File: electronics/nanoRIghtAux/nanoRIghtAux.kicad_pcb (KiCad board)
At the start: 2 copper layers, 16 parts, among them J1 Conn_02x03_Counter_Clockwise, J10 Conn_02x03_Counter_Clockwise, J11 Conn_01x03_Socket, J2 Conn_01x03_Pin, J3 Conn_01x03_Pin, J4 Conn_01x03_Pin, J5 Conn_01x03_Pin, J6 Conn_01x04_Socket, J7 Conn_01x04_Socket, J8 Conn_01x04_Socket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

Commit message: PCB edit started
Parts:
- J1: value Conn_02x03_Counter_Clockwise -> Conn_MM5451
- J10: value Conn_02x03_Counter_Clockwise -> Conn_EA_GLCD
- J11: value Conn_01x03_Socket -> Conn_MAX7219
- J2: value Conn_01x03_Pin -> Conn_HYDA
- J3: value Conn_01x03_Pin -> Conn_HYDB
- J4: value Conn_01x03_Pin -> Conn_FUEL_FR
- J5: value Conn_01x03_Pin -> Conn_FUEL_AL
- J6: value Conn_01x04_Socket -> Conn_MOT_D
- J7: value Conn_01x04_Socket -> Conn_MOT_C
- J8: value Conn_01x04_Socket -> Conn_MOT_B
- J9: value Conn_01x04_Socket -> Conn_MOT_A
- moved SW3 62.9 mm to (199.4, 61.5)
- moved J6 52.6 mm to (223.5, 100.3), turned to 180 degrees
- moved SW2 48.9 mm to (188.9, 65.3), turned to -90 degrees
- moved J10 43.1 mm to (154.9, 85.1), turned to -90 degrees
- moved J7 41.1 mm to (205.7, 121.9), turned to -90 degrees
- moved SW1 41.1 mm to (177.8, 64.8), turned to 180 degrees
- moved J11 40.6 mm to (155.0, 113.0)
- moved J5 39.7 mm to (154.9, 109.2), turned to -90 degrees
- moved J9 39.6 mm to (223.5, 104.1)
- moved J1 35.1 mm to (154.9, 91.4), turned to -90 degrees
- moved J4 33.6 mm to (154.9, 105.4), turned to -90 degrees
- moved J3 27.6 mm to (154.9, 101.6), turned to -90 degrees
- moved U3 26.9 mm to (201.1, 104.8), turned to 180 degrees
- moved J2 21.6 mm to (154.9, 97.8), turned to -90 degrees
- moved J8 18.8 mm to (196.9, 83.8), turned to 90 degrees
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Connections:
- J1 pad 1: unconnected-(J1-Pin_1-Pad1) -> Net-(A1-D4)
- J1 pad 2: unconnected-(J1-Pin_2-Pad2) -> Net-(A1-D5)
- J1 pad 3: Net-(A1-D5) -> +5V
- J1 pad 4: Net-(A1-D4) -> unconnected-(J1-Pin_4-Pad4)
- J1 pad 5: +5V -> GND
- J1 pad 6: GND -> unconnected-(J1-Pin_6-Pad6)
- J10 pad 1: unconnected-(J10-Pin_1-Pad1) -> Net-(A1-D2)
- J10 pad 2: unconnected-(J10-Pin_2-Pad2) -> Net-(A1-D3)
- J10 pad 3: Net-(A1-D3) -> +5V
- J10 pad 4: Net-(A1-D2) -> unconnected-(J10-Pin_4-Pad4)
- J10 pad 5: +5V -> GND
- J10 pad 6: GND -> unconnected-(J10-Pin_6-Pad6)

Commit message: PWR input pinheader added, MAX7219_PWR pinheader added, PCB routing changed
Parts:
- added J12: Conn_PWRInput, Connector_PinHeader_2.54mm:PinHeader_1x02_P2.54mm_Vertical, F.Cu at (147.3, 121.9)
- added J13: Conn_MAX_Pwr, Connector_PinSocket_2.54mm:PinSocket_1x02_P2.54mm_Vertical, F.Cu at (147.3, 115.6)
- SW1, SW2, SW3: footprint Button_Switch_THT:SW_PUSH_6mm -> Connector_PinHeader_2.54mm:PinHeader_1x02_P2.54mm_Vertical
- moved SW3 28.5 mm to (171.4, 67.3)
- moved J7 23.3 mm to (196.8, 100.3), turned to 180 degrees
- moved J8 20.3 mm to (196.8, 104.2), turned to 0 degrees
- moved SW2 12.6 mm to (176.5, 67.3), turned to 0 degrees
- moved SW1 12.5 mm to (166.4, 69.8)
- moved U3 10.2 mm to (210.8, 101.6)
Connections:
- U3 pad 10: Net-(J6-Pin_4) -> Net-(J6-Pin_3)
- U3 pad 11: Net-(J6-Pin_3) -> Net-(J6-Pin_4)
- U3 pad 18: Net-(J7-Pin_3) -> Net-(J7-Pin_4)
- U3 pad 19: Net-(J7-Pin_4) -> Net-(J7-Pin_3)
- U3 pad 24: Net-(J8-Pin_4) -> Net-(J8-Pin_3)
- U3 pad 25: Net-(J8-Pin_3) -> Net-(J8-Pin_4)
- U3 pad 4: Net-(J9-Pin_3) -> Net-(J9-Pin_4)
- U3 pad 5: Net-(J9-Pin_4) -> Net-(J9-Pin_3)
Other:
- board outline added: 101.6 x 94 mm

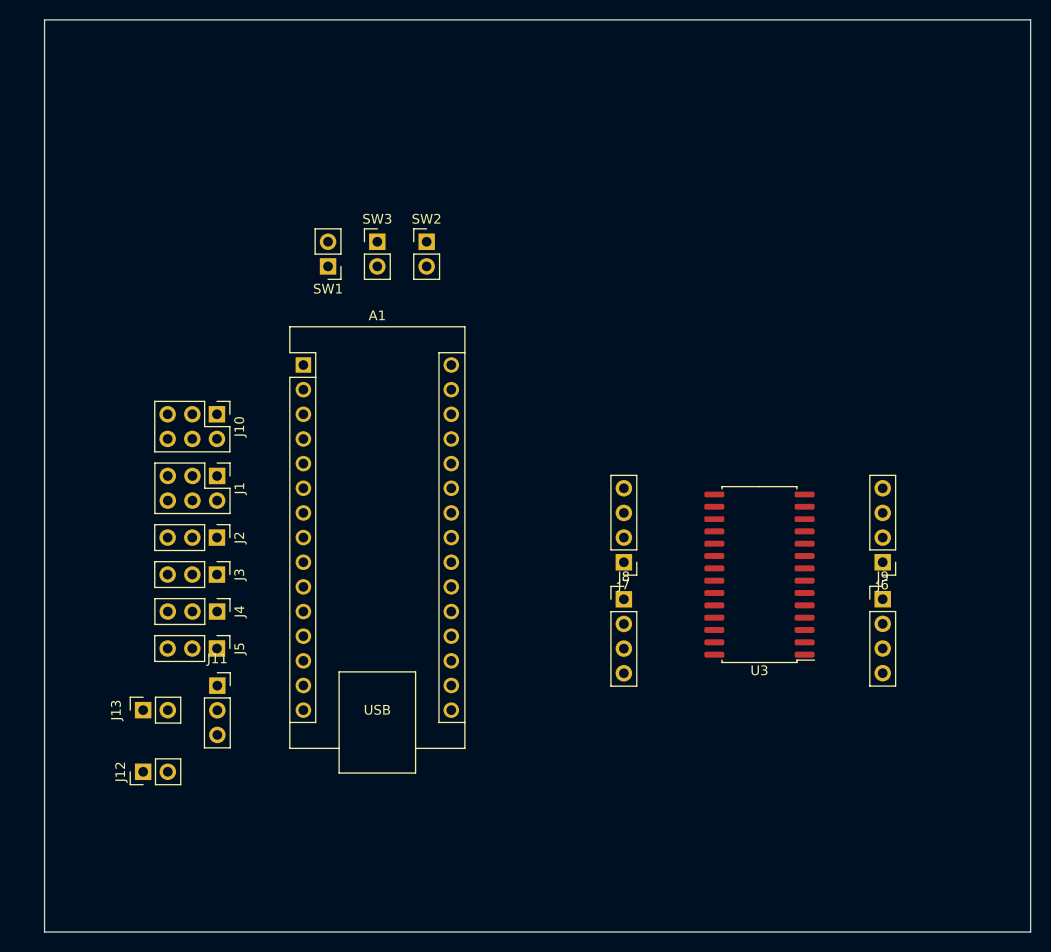
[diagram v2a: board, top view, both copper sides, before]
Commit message: first routing of TH components done.
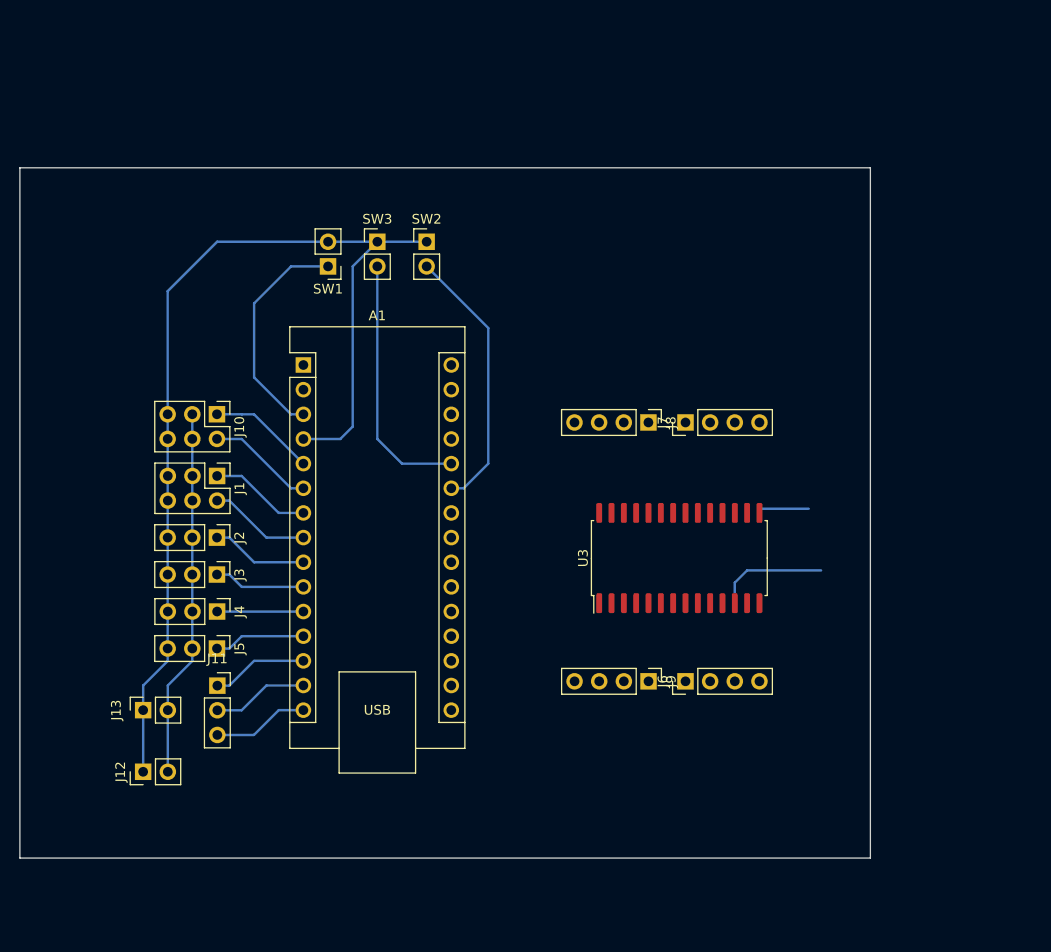
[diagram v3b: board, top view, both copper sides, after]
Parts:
- moved J9 25.6 mm to (199.4, 112.6), turned to -90 degrees
- moved J6 23.7 mm to (203.2, 112.6), turned to 90 degrees
- moved J8 18.4 mm to (199.4, 85.9), turned to -90 degrees
- moved J7 15.7 mm to (203.2, 85.9), turned to 90 degrees
- moved U3 8.43 mm to (202.6, 99.9), turned to 90 degrees
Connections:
- J1 pad 4: unconnected-(J1-Pin_4-Pad4) -> +5V
- J1 pad 6: unconnected-(J1-Pin_6-Pad6) -> GND
- J10 pad 4: unconnected-(J10-Pin_4-Pad4) -> +5V
- J10 pad 6: unconnected-(J10-Pin_6-Pad6) -> GND
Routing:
- net GND: track 0.00 -> 110.1 mm
- net +5V: track 0.00 -> 48.6 mm
- net Net-(A1-A6): track 0.00 -> 27.8 mm
- net Net-(A1-A7): track 0.00 -> 26.5 mm
- net Net-(A1-~{RESET}-Pad3): track 0.00 -> 23.5 mm
- net Net-(A1-D3): track 0.00 -> 11.0 mm
- net Net-(A1-D2): track 0.00 -> 11.0 mm
- net Net-(A1-D5): track 0.00 -> 10.5 mm
- net Net-(A1-D4): track 0.00 -> 10.5 mm
- net Net-(A1-D6): track 0.00 -> 9.96 mm
- net Net-(A1-D12): track 0.00 -> 9.92 mm
- net Net-(A1-D10): track 0.00 -> 9.92 mm
- net Net-(A1-D11): track 0.00 -> 9.92 mm
- net Net-(A1-D7): track 0.00 -> 9.43 mm
- net Net-(A1-D9): track 0.00 -> 9.43 mm
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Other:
- board size 101.6 x 94 mm -> 87.6 x 71.1 mm

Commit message: routing cleanup of TH components
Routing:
- net +5V: track 48.6 -> 37.9 mm
- net GND: track 110.1 -> 105.1 mm
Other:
- board text added: "RightAUX Control Board"
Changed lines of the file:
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@@
     (pad_to_mask_clearance 0)
     (pcbplotparams
-      (layerselection 0x00010fc_ffffffff)
+      (layerselection 0x0000000_fffffffe)
       (plot_on_all_layers_selection 0x0000000_00000000)
       (disableapertmacros false)
@@
       (outputformat 1)
       (mirror false)
-      (drillshape 1)
+      (drillshape 0)
       (scaleselection 1)
-      (outputdirectory "")
+      (outputdirectory "/media/michi/miWorkdata/myproject/F-16SimulatorParts/BMSAIT-RightAux/electronics/nanoRIghtAux/")
     )
   )
@@
   (gr_rect (start 134.62 59.69) (end 222.25 130.81)
     (stroke (width 0.1) (type default)) (fill none) (layer "Edge.Cuts"))
+  (gr_text "RightAUX Control Board" (at 161.29 127) (layer "B.SilkS")
+    (effects (font (size 2 2) (thickness 0.15)) (justify left bottom))
+  )
   (segment (start 166.37 69.85) (end 162.56 69.85) (width 0.25) (layer "B.Cu") (net 3))
   (segment (start 158.75 81.28) (end 158.75 73.66) (width 0.25) (layer "B.Cu") (net 3))
@@
   (segment (start 171.45 67.31) (end 168.91 69.85) (width 0.25) (layer "B.Cu") (net 4))
   (segment (start 166.37 67.31) (end 154.94 67.31) (width 0.25) (layer "B.Cu") (net 4))
-  (segment (start 215.9 94.82) (end 210.82 94.82) (width 0.25) (layer "B.Cu") (net 4))
   (segment (start 149.845 110.505) (end 147.32 113.03) (width 0.25) (layer "B.Cu") (net 4))
   (segment (start 168.91 69.85) (end 168.91 86.36) (width 0.25) (layer "B.Cu") (net 4))
@@
   (segment (start 171.45 87.63) (end 173.99 90.17) (width 0.25) (layer "B.Cu") (net 26))
   (segment (start 173.99 90.17) (end 179.07 90.17) (width 0.25) (layer "B.Cu") (net 26))
-  (segment (start 217.17 101.17) (end 209.55 101.17) (width 0.25) (layer "B.Cu") (net 30))
   (segment (start 152.385 85.085) (end 152.385 109.22) (width 0.25) (layer "B.Cu") (net 30))
   (segment (start 152.385 110.505) (end 149.86 113.03) (width 0.25) (layer "B.Cu") (net 30))
-  (segment (start 208.28 102.44) (end 208.28 103.71) (width 0.25) (layer "B.Cu") (net 30))
-  (segment (start 209.55 101.17) (end 208.28 102.44) (width 0.25) (layer "B.Cu") (net 30))
   (segment (start 149.86 113.03) (end 149.86 121.92) (width 0.25) (layer "B.Cu") (net 30))
   (segment (start 152.385 109.22) (end 152.385 110.505) (width 0.25) (layer "B.Cu") (net 30))

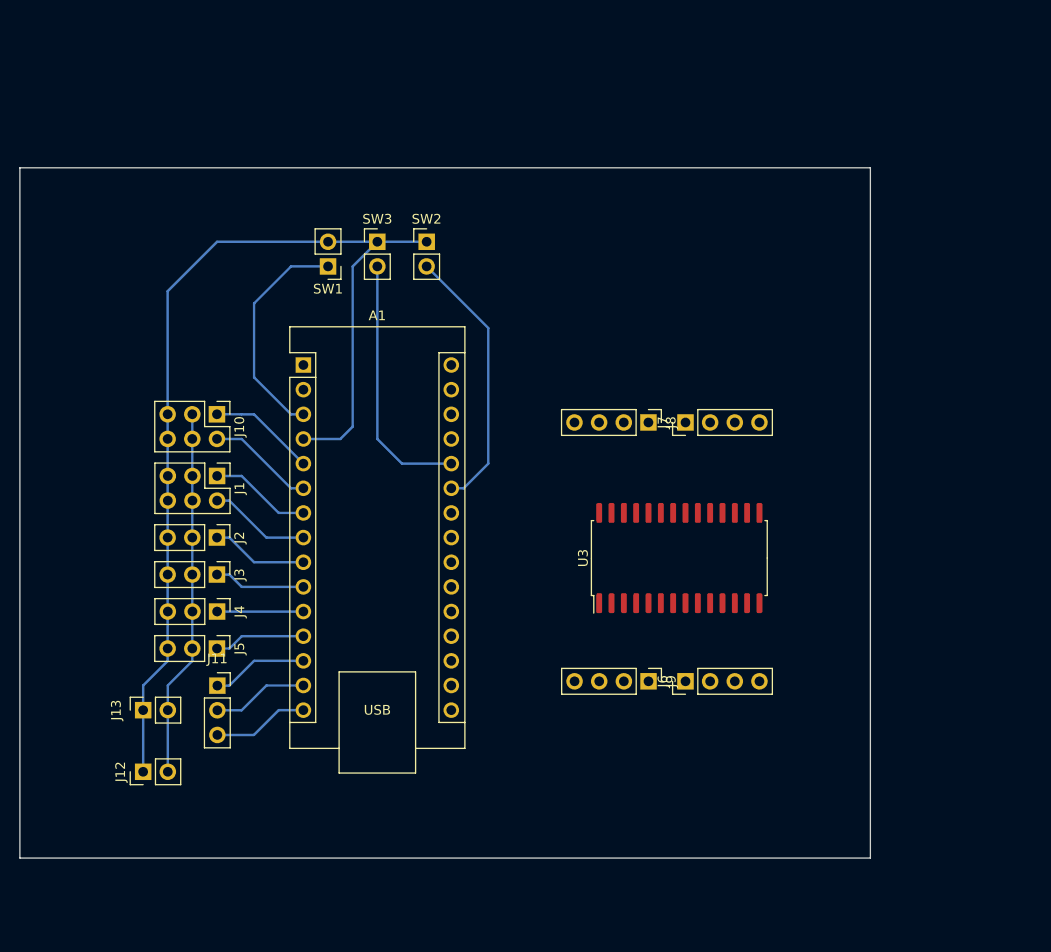
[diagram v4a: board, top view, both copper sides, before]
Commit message: mountingholes addes
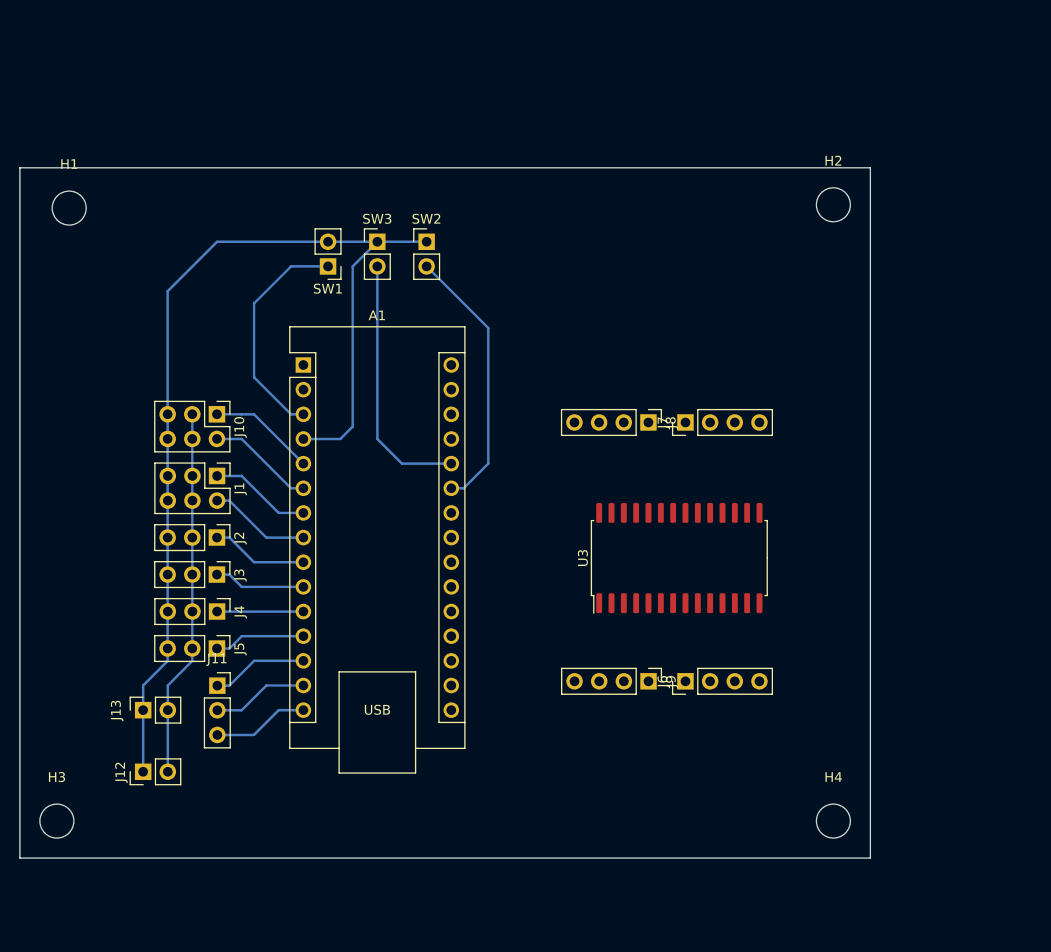
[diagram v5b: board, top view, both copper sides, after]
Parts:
- added H1: MountingHole, MountingHole:MountingHole_3.5mm, F.Cu at (139.7, 63.8)
- added H2: MountingHole, MountingHole:MountingHole_3.5mm, F.Cu at (218.4, 63.5)
- added H3: MountingHole, MountingHole:MountingHole_3.5mm, F.Cu at (138.4, 127.0)
- added H4: MountingHole, MountingHole:MountingHole_3.5mm, F.Cu at (218.4, 127.0)
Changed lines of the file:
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@@
     )
+  )
+  (footprint "MountingHole:MountingHole_3.5mm" (layer "F.Cu")
+    (at 139.7 63.84)
+    (descr "Mounting Hole 3.5mm, no annular")
+    (tags "mounting hole 3.5mm no annular")
+    (property "Sheetfile" "nanoRIghtAux.kicad_sch")
+    (property "Sheetname" "")
+    (property "ki_description" "Mounting Hole without connection")
+    (property "ki_keywords" "mounting hole")
+    (attr exclude_from_pos_files)
+    (fp_text reference "H1" (at 0 -4.5) (layer "F.SilkS")
+        (effects (font (size 1 1) (thickness 0.15)))
+    )
+    (fp_text value "MountingHole" (at 0 4.5) (layer "F.Fab")
+        (effects (font (size 1 1) (thickness 0.15)))
+    )
+    (fp_text user "${REFERENCE}" (at 0 0) (layer "F.Fab")
+        (effects (font (size 1 1) (thickness 0.15)))
+    )
+    (fp_circle (center 0 0) (end 3.5 0)
+      (stroke (width 0.15) (type solid)) (fill none) (layer "Cmts.User"))
+    (fp_circle (center 0 0) (end 3.75 0)
+      (stroke (width 0.05) (type solid)) (fill none) (layer "F.CrtYd"))
+    (pad "" np_thru_hole circle (at 0 0) (size 3.5 3.5) (drill 3.5) (layers "*.Cu" "*.Mask"))
   )
   (footprint "Connector_PinHeader_2.54mm:PinHeader_1x04_P2.54mm_Vertical" (layer "F.Cu")
@@
       (rotate (xyz 0 0 0))
     )
+  )
+  (footprint "MountingHole:MountingHole_3.5mm" (layer "F.Cu")
+    (at 218.44 127)
+    (descr "Mounting Hole 3.5mm, no annular")
+    (tags "mounting hole 3.5mm no annular")
+    (property "Sheetfile" "nanoRIghtAux.kicad_sch")
+    (property "Sheetname" "")
+    (property "ki_description" "Mounting Hole without connection")
+    (property "ki_keywords" "mounting hole")
+    (attr exclude_from_pos_files)
+    (fp_text reference "H4" (at 0 -4.5) (layer "F.SilkS")
+        (effects (font (size 1 1) (thickness 0.15)))
+    )
+    (fp_text value "MountingHole" (at 0 4.5) (layer "F.Fab")
+        (effects (font (size 1 1) (thickness 0.15)))
+    )
+    (fp_text user "${REFERENCE}" (at 0 0) (layer "F.Fab")
+        (effects (font (size 1 1) (thickness 0.15)))
+    )
+    (fp_circle (center 0 0) (end 3.5 0)
+      (stroke (width 0.15) (type solid)) (fill none) (layer "Cmts.User"))
+    (fp_circle (center 0 0) (end 3.75 0)
+      (stroke (width 0.05) (type solid)) (fill none) (layer "F.CrtYd"))
+    (pad "" np_thru_hole circle (at 0 0) (size 3.5 3.5) (drill 3.5) (layers "*.Cu" "*.Mask"))
   )
   (footprint "Connector_PinHeader_2.54mm:PinHeader_1x04_P2.54mm_Vertical" (layer "F.Cu")
@@
     )
   )
+  (footprint "MountingHole:MountingHole_3.5mm" (layer "F.Cu")
+    (at 218.44 63.5)
+    (descr "Mounting Hole 3.5mm, no annular")
+    (tags "mounting hole 3.5mm no annular")
+    (property "Sheetfile" "nanoRIghtAux.kicad_sch")
+    (property "Sheetname" "")
+    (property "ki_description" "Mounting Hole without connection")
+    (property "ki_keywords" "mounting hole")
+    (attr exclude_from_pos_files)
+    (fp_text reference "H2" (at 0 -4.5) (layer "F.SilkS")
+        (effects (font (size 1 1) (thickness 0.15)))
+    )
+    (fp_text value "MountingHole" (at 0 4.5) (layer "F.Fab")
+        (effects (font (size 1 1) (thickness 0.15)))
+    )
+    (fp_text user "${REFERENCE}" (at 0 0) (layer "F.Fab")
+        (effects (font (size 1 1) (thickness 0.15)))
+    )
+    (fp_circle (center 0 0) (end 3.5 0)
+      (stroke (width 0.15) (type solid)) (fill none) (layer "Cmts.User"))
+    (fp_circle (center 0 0) (end 3.75 0)
+      (stroke (width 0.05) (type solid)) (fill none) (layer "F.CrtYd"))
+    (pad "" np_thru_hole circle (at 0 0) (size 3.5 3.5) (drill 3.5) (layers "*.Cu" "*.Mask"))
+  )
+  (footprint "MountingHole:MountingHole_3.5mm" (layer "F.Cu")
+    (at 138.43 127)
+    (descr "Mounting Hole 3.5mm, no annular")
+    (tags "mounting hole 3.5mm no annular")
+    (property "Sheetfile" "nanoRIghtAux.kicad_sch")
+    (property "Sheetname" "")
+    (property "ki_description" "Mounting Hole without connection")
+    (property "ki_keywords" "mounting hole")
+    (attr exclude_from_pos_files)
+    (fp_text reference "H3" (at 0 -4.5) (layer "F.SilkS")
+        (effects (font (size 1 1) (thickness 0.15)))
+    )
+    (fp_text value "MountingHole" (at 0 4.5) (layer "F.Fab")
+        (effects (font (size 1 1) (thickness 0.15)))
+    )
+    (fp_text user "${REFERENCE}" (at 0 0) (layer "F.Fab")
+        (effects (font (size 1 1) (thickness 0.15)))
+    )
+    (fp_circle (center 0 0) (end 3.5 0)
+      (stroke (width 0.15) (type solid)) (fill none) (layer "Cmts.User"))
+    (fp_circle (center 0 0) (end 3.75 0)
+      (stroke (width 0.05) (type solid)) (fill none) (layer "F.CrtYd"))
+    (pad "" np_thru_hole circle (at 0 0) (size 3.5 3.5) (drill 3.5) (layers "*.Cu" "*.Mask"))
+  )
   (footprint "Connector_PinHeader_2.54mm:PinHeader_1x03_P2.54mm_Vertical" (layer "F.Cu")
